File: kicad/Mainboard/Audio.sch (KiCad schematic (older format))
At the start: 44 parts, among them J10 SPK_INT, J11 SPK_EXT, J8 MIC_INT, J9 MIC_EXT, SW1 INT_PTT_SW, U7 OPA340UA, U8 LM386

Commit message: Updated WIP schematics
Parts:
- added C?: 47n, symbol Device:C_Small
- C50: value 10u -> 22u
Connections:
- net PTT_INT is gone; now on net PTT: R13.2
- net +3V3: now also R15.1; no longer SW1.1
- net ADC1_0: now also C?.2
- net GND: now also SW1.2; no longer R15.2
- net at C48.2, R13.1: now also R15.2, SW1.1; no longer R15.1, SW1.2
- net at R16.1, R17.1, U7.2 (-): now also C?.1
- net PTT_EXT renamed PTT
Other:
- moved on the sheet: C48, R13, R15, SW1
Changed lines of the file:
@@
 P 1900 3100
 F 0 "C50" H 1992 3146 50  0000 L CNN
-F 1 "10u" H 1992 3055 50  0000 L CNN
+F 1 "22u" H 1992 3055 50  0000 L CNN
 F 2 "" H 1900 3100 50  0001 C CNN
 F 3 "~" H 1900 3100 50  0001 C CNN
@@
 	1800 1800 1900 1800
 Wire Wire Line
-	1550 2600 1900 2600
+	1550 2600 1650 2600
 Wire Wire Line
 	1900 1800 1900 2600
 Connection ~ 1900 2600
 Wire Wire Line
-	1000 2600 1350 2600
+	1000 2600 1250 2600
 $Comp
 L power:GND #PWR084
@@
 L Mainboard-rescue:SW_Push-switches SW1
 U 1 1 5DFE1B21
-P 10200 1200
-F 0 "SW1" V 10154 1348 50  0000 L CNN
-F 1 "INT_PTT_SW" V 10245 1348 50  0000 L CNN
-F 2 "" H 10200 1400 50  0001 C CNN
-F 3 "" H 10200 1400 50  0001 C CNN
-	1    10200 1200
+P 10200 1600
+F 0 "SW1" V 10154 1748 50  0000 L CNN
+F 1 "INT_PTT_SW" V 10245 1748 50  0000 L CNN
+F 2 "" H 10200 1800 50  0001 C CNN
+F 3 "" H 10200 1800 50  0001 C CNN
+	1    10200 1600
 	0    1    1    0
 $EndComp
@@
 L Mainboard-rescue:R_Small-device R15
 U 1 1 5DFE1F5D
-P 10200 1700
-F 0 "R15" H 10259 1746 50  0000 L CNN
-F 1 "10k" H 10259 1655 50  0000 L CNN
-F 2 "" H 10200 1700 50  0001 C CNN
-F 3 "~" H 10200 1700 50  0001 C CNN
-	1    10200 1700
+P 10200 1200
+F 0 "R15" H 10259 1246 50  0000 L CNN
+F 1 "10k" H 10259 1155 50  0000 L CNN
+F 2 "" H 10200 1200 50  0001 C CNN
+F 3 "~" H 10200 1200 50  0001 C CNN
+	1    10200 1200
 	1    0    0    -1
 $EndComp
@@
 L power:+3V3 #PWR078
 U 1 1 5DFE2751
-P 10200 900
-F 0 "#PWR078" H 10200 750 50  0001 C CNN
-F 1 "+3V3" H 10215 1073 50  0000 C CNN
-F 2 "" H 10200 900 50  0001 C CNN
-F 3 "" H 10200 900 50  0001 C CNN
-	1    10200 900
+P 10200 1000
+F 0 "#PWR078" H 10200 850 50  0001 C CNN
+F 1 "+3V3" H 10215 1173 50  0000 C CNN
+F 2 "" H 10200 1000 50  0001 C CNN
+F 3 "" H 10200 1000 50  0001 C CNN
+	1    10200 1000
 	1    0    0    -1
 $EndComp
@@
 L Mainboard-rescue:C_Small-device C48
 U 1 1 5DFE4F3F
-P 9850 1700
-F 0 "C48" H 9758 1654 50  0000 R CNN
-F 1 "100n" H 9758 1745 50  0000 R CNN
-F 2 "" H 9850 1700 50  0001 C CNN
-F 3 "~" H 9850 1700 50  0001 C CNN
-	1    9850 1700
+P 9850 1600
+F 0 "C48" H 9758 1554 50  0000 R CNN
+F 1 "100n" H 9758 1645 50  0000 R CNN
+F 2 "" H 9850 1600 50  0001 C CNN
+F 3 "~" H 9850 1600 50  0001 C CNN
+	1    9850 1600
 	-1   0    0    1
 $EndComp
@@
 $EndComp
 Wire Wire Line
-	9550 1500 9450 1500
-Text GLabel 9450 1500 0    50   Input ~ 10
-PTT_INT
+	9550 1400 9450 1400
+Text GLabel 9450 1400 0    50   Input ~ 10
+PTT
 $Comp
 L Mainboard-rescue:Conn_01x02-conn J10
@@
 	800  6600 800  6700
 Wire Wire Line
-	10200 900  10200 1000
-Wire Wire Line
-	9850 1800 9850 1900
-Wire Wire Line
-	10200 1400 10200 1500
-Wire Wire Line
-	10200 1500 9850 1500
-Wire Wire Line
-	9850 1500 9850 1600
-Connection ~ 10200 1500
-Wire Wire Line
-	10200 1500 10200 1600
+	10200 1000 10200 1100
+Wire Wire Line
+	10200 1400 9850 1400
+Wire Wire Line
+	9850 1400 9850 1500
 $Comp
 L Mainboard-rescue:R_Small-device R13
 U 1 1 5DF5BF76
-P 9650 1500
-F 0 "R13" V 9454 1500 50  0000 C CNN
-F 1 "470" V 9545 1500 50  0000 C CNN
-F 2 "" H 9650 1500 50  0001 C CNN
-F 3 "~" H 9650 1500 50  0001 C CNN
-	1    9650 1500
+P 9650 1400
+F 0 "R13" V 9454 1400 50  0000 C CNN
+F 1 "470" V 9545 1400 50  0000 C CNN
+F 2 "" H 9650 1400 50  0001 C CNN
+F 3 "~" H 9650 1400 50  0001 C CNN
+	1    9650 1400
 	0    1    1    0
 $EndComp
 Wire Wire Line
-	9750 1500 9850 1500
-Connection ~ 9850 1500
+	9750 1400 9850 1400
+Connection ~ 9850 1400
 Text Notes 8900 2250 0    50   ~ 10
 Pushing PTT on power up forces STM32 into DFU mode
@@
 	8250 3750 8350 3750
 Text GLabel 8350 3750 2    50   Input ~ 10
-PTT_EXT
+PTT
 $Comp
 L Mainboard-rescue:C_Small-device C54
@@
 Wire Wire Line
 	4200 5300 4200 5800
+$Comp
+L Device:C_Small C?
+U 1 1 5E069A61
+P 1450 2950
+F 0 "C?" V 1221 2950 50  0000 C CNN
+F 1 "47n" V 1312 2950 50  0000 C CNN
+F 2 "" H 1450 2950 50  0001 C CNN
+F 3 "~" H 1450 2950 50  0001 C CNN
+	1    1450 2950
+	0    1    1    0
+$EndComp
+Wire Wire Line
+	1550 2950 1650 2950
+Wire Wire Line
+	1650 2950 1650 2600
+Connection ~ 1650 2600
+Wire Wire Line
+	1650 2600 1900 2600
+Wire Wire Line
+	1350 2950 1250 2950
+Wire Wire Line
+	1250 2950 1250 2600
+Connection ~ 1250 2600
+Wire Wire Line
+	1250 2600 1350 2600
+Wire Wire Line
+	10200 1400 10200 1300
+Connection ~ 10200 1400
+Wire Wire Line
+	9850 1700 9850 1900
 $EndSCHEMATC

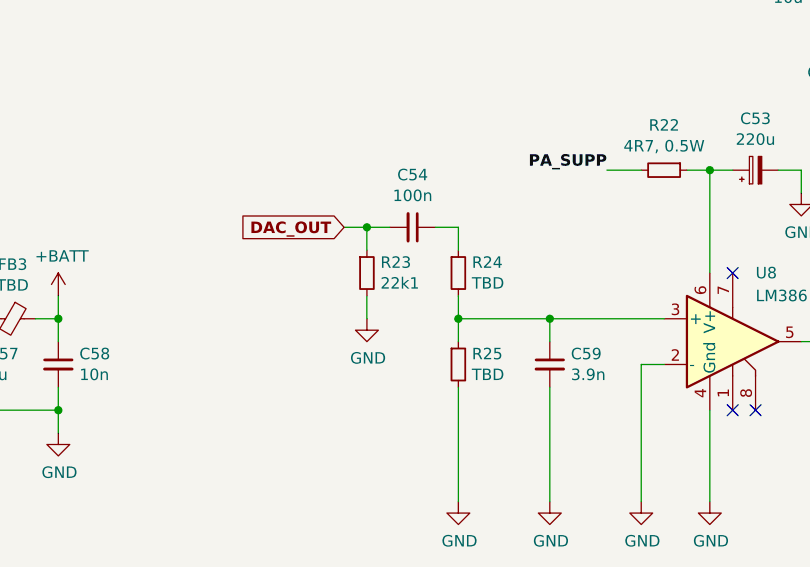
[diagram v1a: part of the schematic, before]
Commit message: Add files via upload
* replaced Q7 with BSS138
* new HMI connector (for keypad and display)
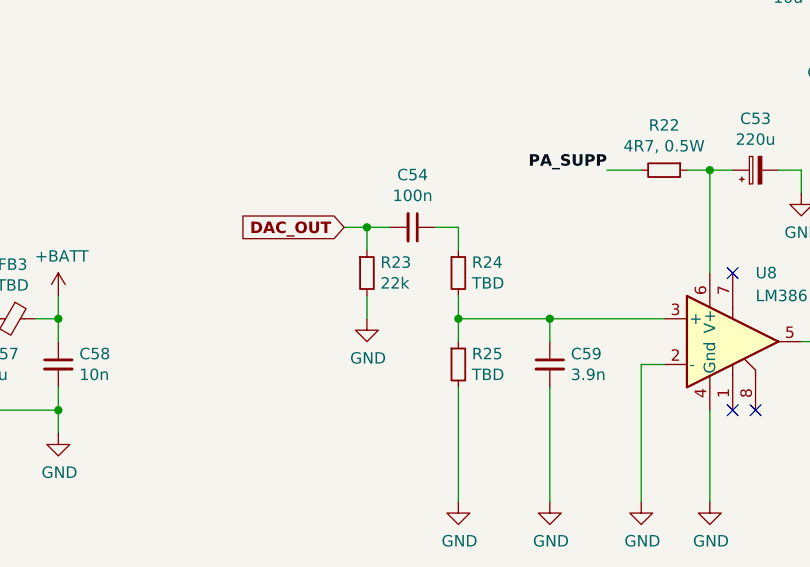
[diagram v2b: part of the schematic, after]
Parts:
- R23: value 22k1 -> 22k
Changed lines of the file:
@@
 EESchema Schematic File Version 4
+LIBS:Mainboard-cache
 EELAYER 30 0
 EELAYER END
@@
 P 3800 4800
 F 0 "R23" H 3859 4846 50  0000 L CNN
-F 1 "22k1" H 3859 4755 50  0000 L CNN
+F 1 "22k" H 3859 4755 50  0000 L CNN
 F 2 "" H 3800 4800 50  0001 C CNN
 F 3 "~" H 3800 4800 50  0001 C CNN

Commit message: Annotated parts
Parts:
- gave numbers to parts that had none: 1
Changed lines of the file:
@@
 	4200 5300 4200 5800
 $Comp
-L Device:C_Small C?
+L Device:C_Small C87
 U 1 1 5E069A61
 P 1450 2950
-F 0 "C?" V 1221 2950 50  0000 C CNN
+F 0 "C87" V 1221 2950 50  0000 C CNN
 F 1 "47n" V 1312 2950 50  0000 C CNN
 F 2 "" H 1450 2950 50  0001 C CNN

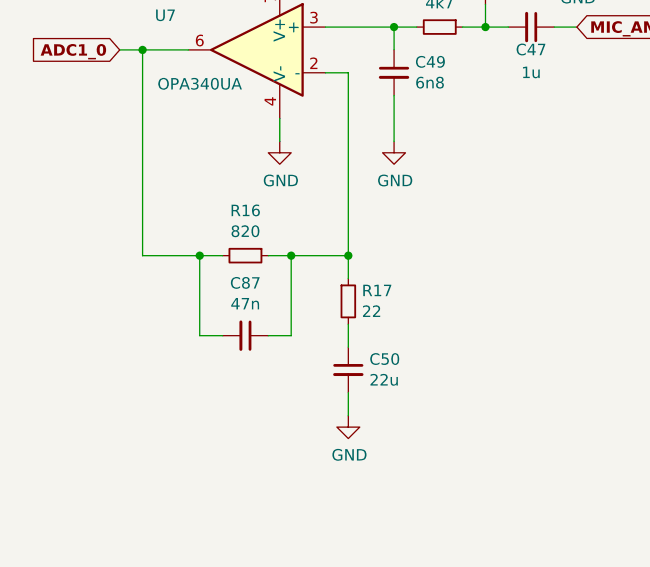
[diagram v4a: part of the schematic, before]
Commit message: Revert "Annotated parts"
This reverts commit b309e3bfe0d7a41f96c10818008ed221b92f9604.
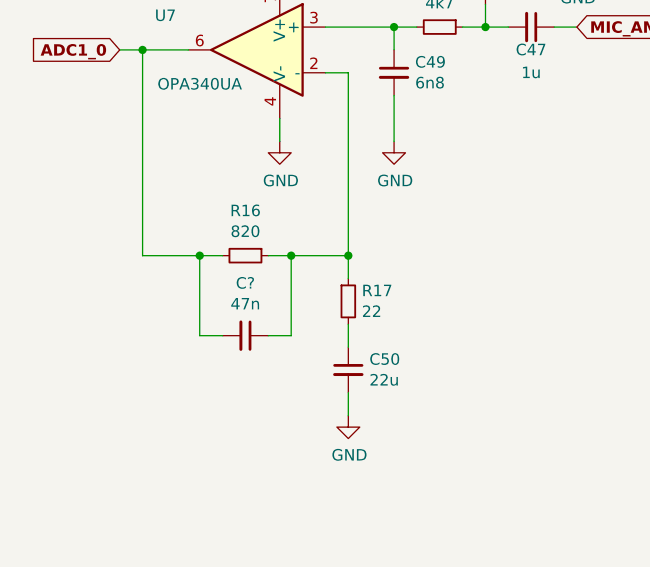
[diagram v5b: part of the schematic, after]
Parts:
- renumbered C87 to C?
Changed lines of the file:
@@
 	4200 5300 4200 5800
 $Comp
-L Device:C_Small C87
+L Device:C_Small C?
 U 1 1 5E069A61
 P 1450 2950
-F 0 "C87" V 1221 2950 50  0000 C CNN
+F 0 "C?" V 1221 2950 50  0000 C CNN
 F 1 "47n" V 1312 2950 50  0000 C CNN
 F 2 "" H 1450 2950 50  0001 C CNN

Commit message: Add files via upload
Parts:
- removed C54: 100n, symbol Mainboard-rescue:C_Small-device
- removed R22: 4R7, 0.5W, symbol Mainboard-rescue:R_Small-device
- removed R23: 22k, symbol Mainboard-rescue:R_Small-device
- added C?: 220n, symbol Mainboard-rescue:C_Small-device
- added RV?: 50k/log, symbol Device:R_POT
- C59: value 3.9n -> 15n
- R24: value TBD -> 22k
- renumbered R25 to 2k2
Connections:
- net PA_SUPP is gone; now on an unnamed net: C56.1, C57.1, FB3.2
- net GND: now also RV?.3
- net at R24.1: now also 2k2.1, C59.1, C?.1
- new net: RV?.2, U8.3 (+)
- new net: C?.2, RV?.1
- new net AUDIO_DAC: R24.2
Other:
- note added: "0.5W"
- moved on the sheet: 2k2, C46, C47, C49, C50, C51, C52, C53, C55, C56, C57, C58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

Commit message: Add files via upload
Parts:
- added C?: 100n, symbol Device:C_Small
- added C?: 10n, symbol Mainboard-rescue:C_Small-device
- added C?: 1u, symbol Mainboard-rescue:C_Small-device
- added C?: 100n, symbol Mainboard-rescue:C_Small-device
- added FB?: TBD, symbol Mainboard-rescue:Ferrite_Bead_Small-device
- added Q? (x2): BSS138-transistors, TO_SOT_Packages_SMD:SOT-23, symbol Mainboard-rescue:BSS138-transistors
- added R? (x2): 22k, symbol Mainboard-rescue:R_Small-device
- added R?: TBF, symbol Mainboard-rescue:R_Small-device
- added R? (x2): 47k, symbol Mainboard-rescue:R_Small-device
- added U? (x5): 4066, symbol 4xxx:4066
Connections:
- net +3V3: now also R?.1
- net +BATT: now also C?.1, FB?.1, R?.1, R?.1
- net AUDIO_DAC: now also U?.1, U?.4; no longer R24.2
- net GND: now also C?.2, C?.2, C?.2, Q?.2 (S), Q?.2 (S), R?.2, U?.12, U?.6, U?.7 (VSS)
- new net: C?.1, R?.2
- new net: Q?.3 (D), R?.2, U?.13
- new net: Q?.3 (D), R?.2, U?.5
- new net: C?.1, C?.1, FB?.2, U?.14 (VDD)
- new net ADC3_1: R?.1, R?.1, R?.2
- new net ADF_SWD: C?.2
- new net FM_MOD: U?.2
- new net FM_MOD_SEL: Q?.1 (G)
- new net SPK_AMP: R24.2, U?.3
- new net SPK_AMP_SEL: Q?.1 (G)
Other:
- note added: "This circuit provides attenuation and adds DC component\nto the analog FM demod output"
- moved on the sheet: C46, C47, C49, C50, C?, D2, D3, R10, R11, R12, R14, R16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
